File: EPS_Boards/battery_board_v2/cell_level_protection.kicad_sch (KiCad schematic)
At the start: 32 parts, among them J8 Shunt Resistor, Q10 CSD16401Q5, Q3 CSD16401Q5, Q4 CSD16401Q5, Q5 CSD16401Q5, Q6 CSD16401Q5, Q7 CSD16401Q5, Q8 CSD16401Q5, Q9 CSD16401Q5, U10 BQ297xx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

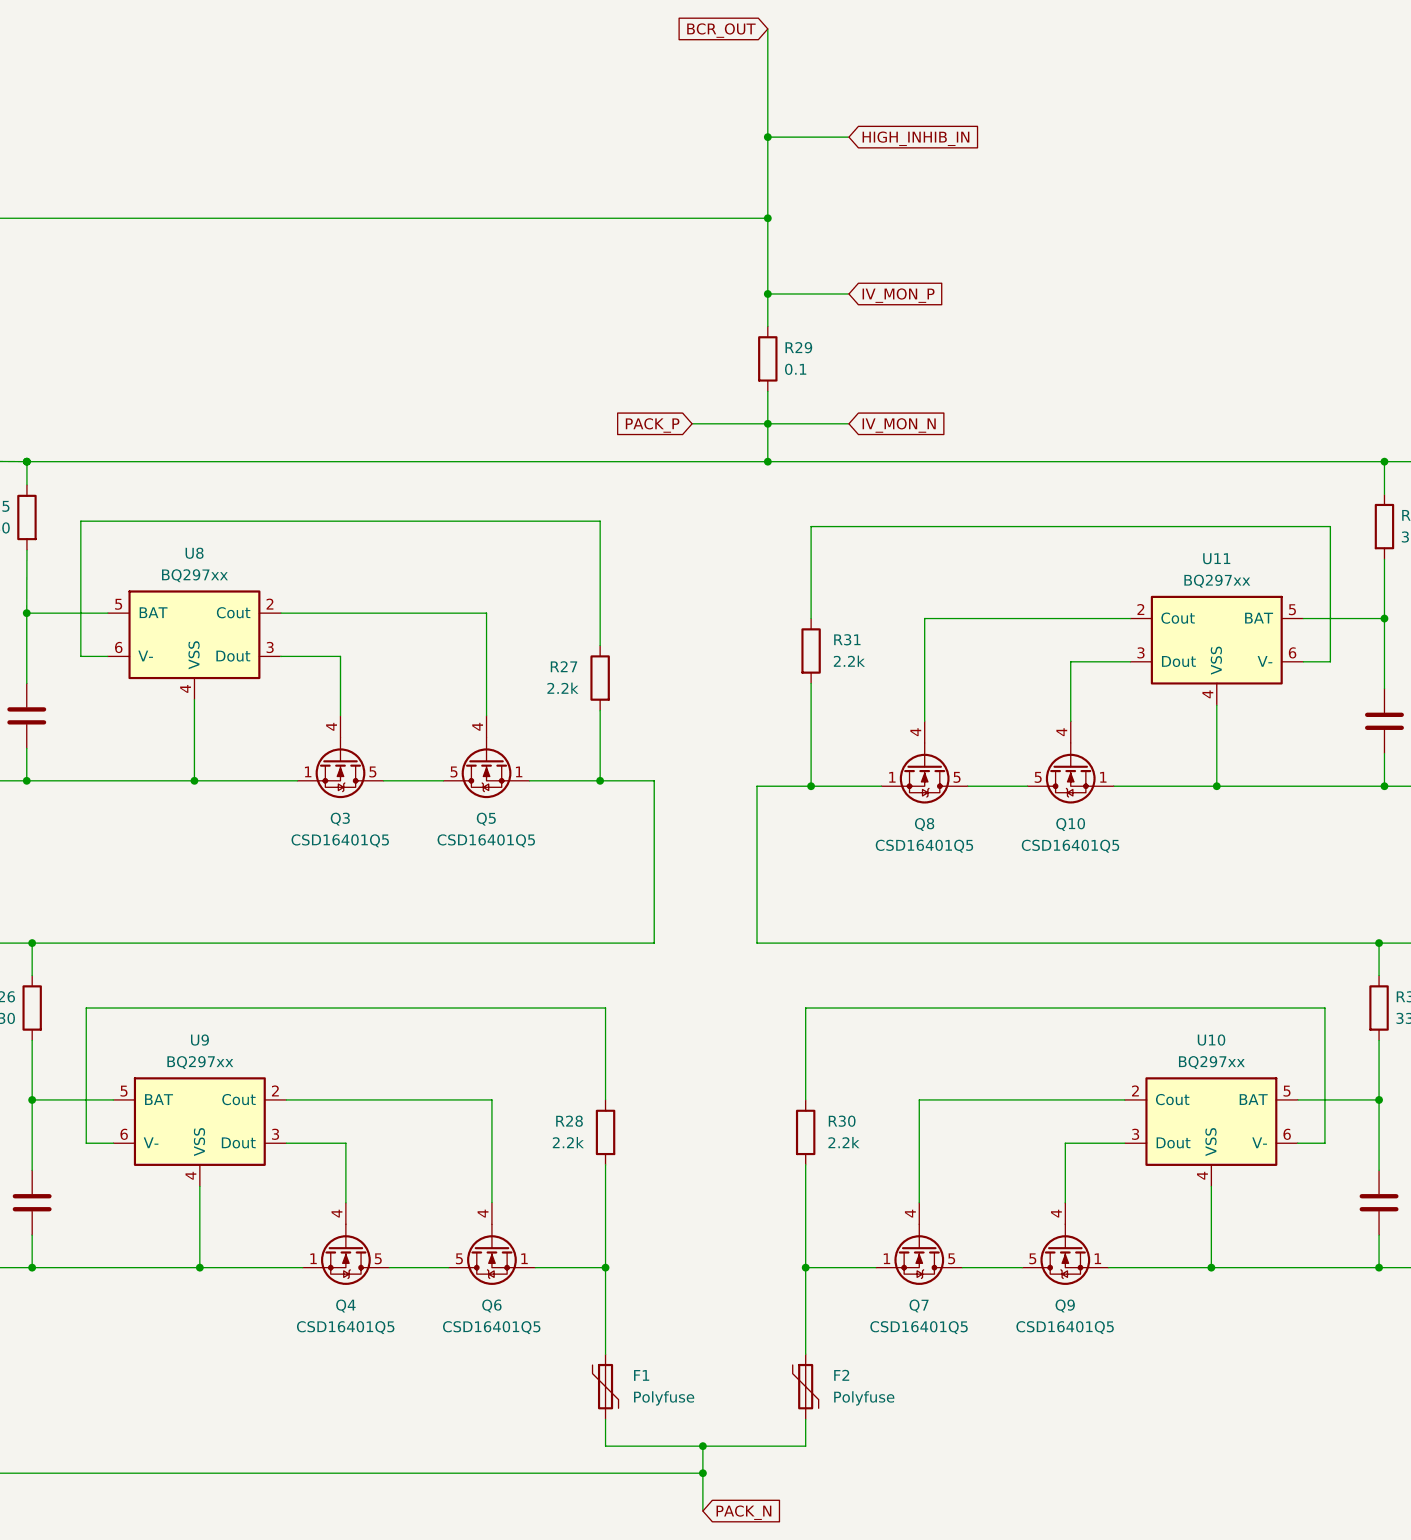
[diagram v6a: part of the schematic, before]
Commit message: eps: battery board: updated board layout
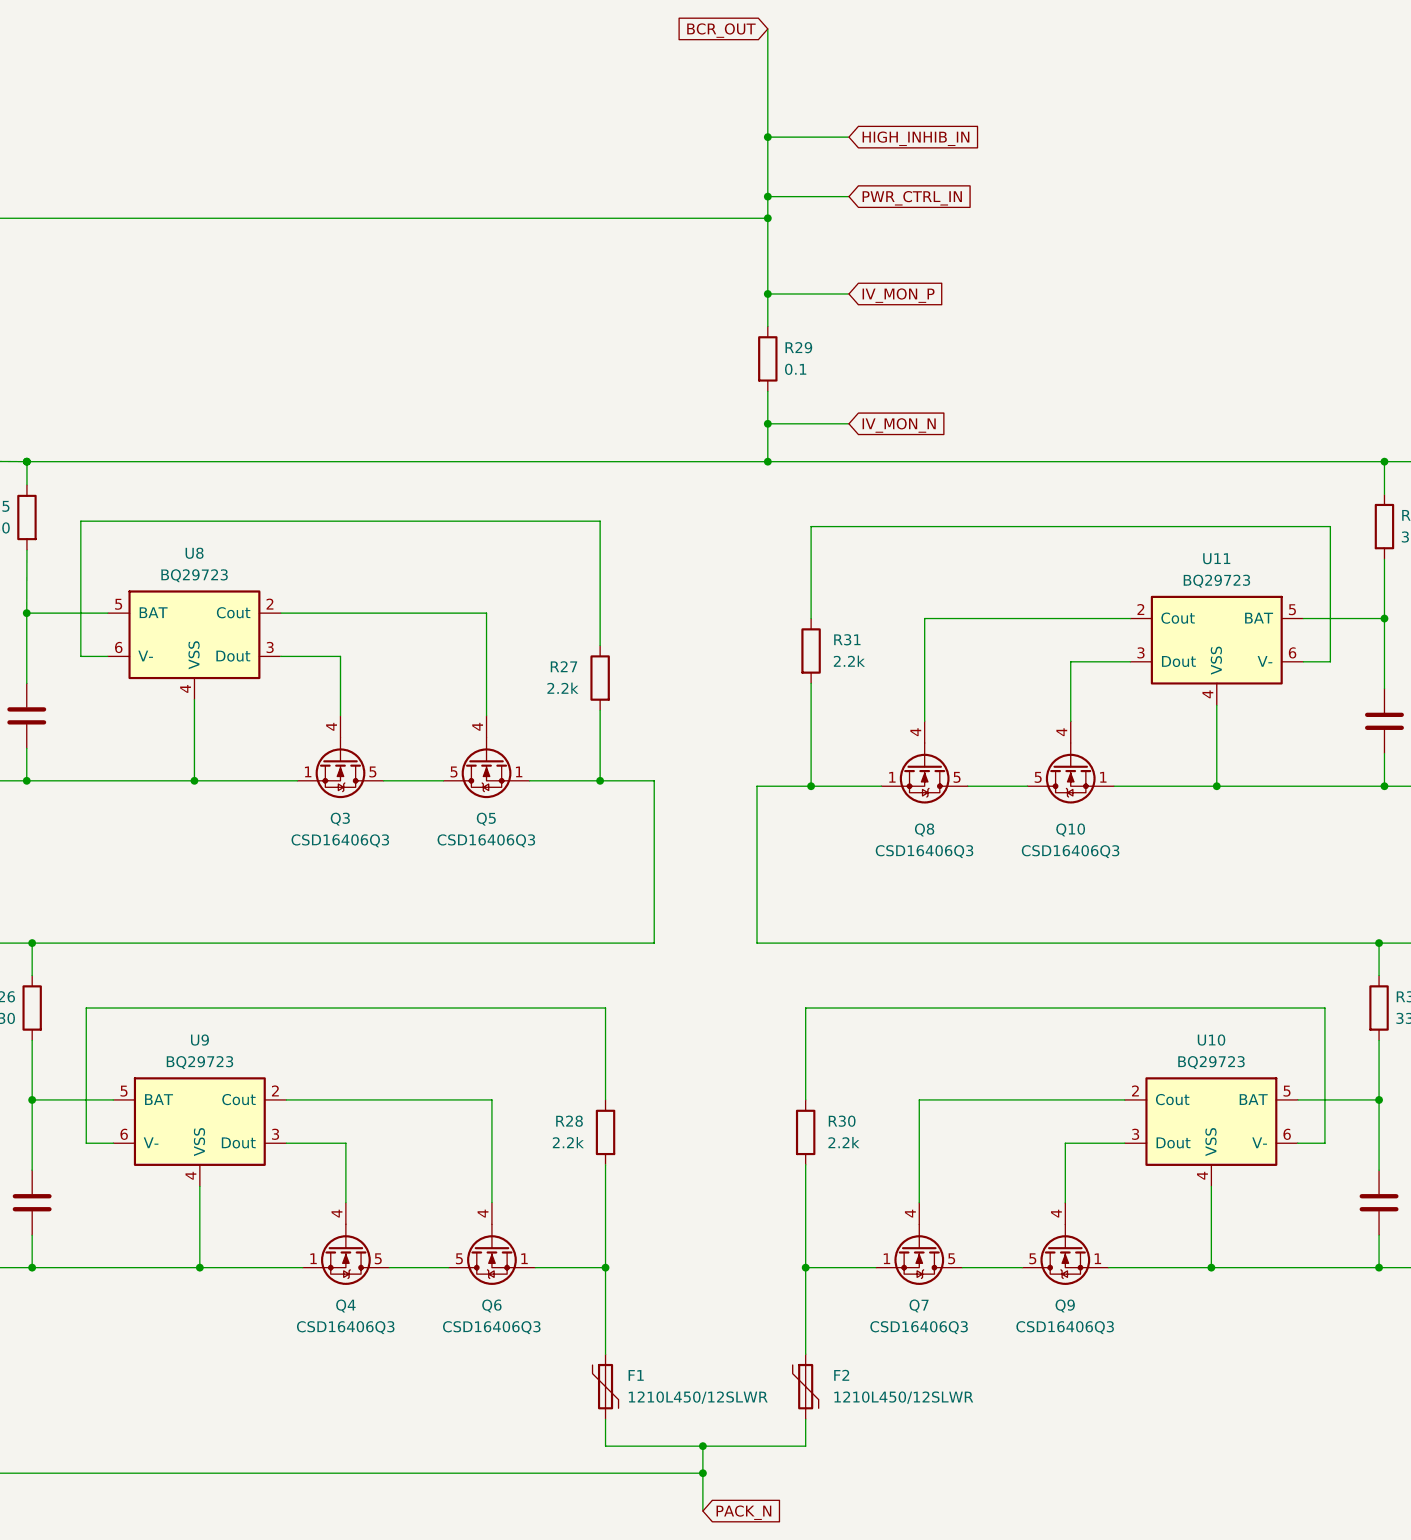
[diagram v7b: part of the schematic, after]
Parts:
- F1, F2: value Polyfuse -> 1210L450/12SLWR
- Q10, Q3, Q4, Q5, Q6, Q7, Q8, Q9: value CSD16401Q5 -> CSD16406Q3
- U10, U11, U8, U9: value BQ297xx -> BQ29723
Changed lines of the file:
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@@
   (junction (at 140.97 181.61) (diameter 0) (color 0 0 0 0)
   )
+  (junction (at 227.33 75.565) (diameter 0) (color 0 0 0 0)
+  )
   (junction (at 299.085 201.295) (diameter 0) (color 0 0 0 0)
   )
@@
     (stroke (width 0) (type default) (color 0 0 0 0))
   )
-  (wire (pts (xy 227.33 68.58) (xy 227.33 78.105))
+  (wire (pts (xy 227.33 68.58) (xy 227.33 75.565))
     (stroke (width 0) (type default) (color 0 0 0 0))
   )
@@
     (stroke (width 0) (type default) (color 0 0 0 0))
   )
+  (wire (pts (xy 227.33 75.565) (xy 236.855 75.565))
+    (stroke (width 0) (type default) (color 0 0 0 0))
+  )
   (wire (pts (xy 232.41 144.78) (xy 240.665 144.78))
     (stroke (width 0) (type default) (color 0 0 0 0))
@@
     (stroke (width 0) (type default) (color 0 0 0 0))
   )
+  (wire (pts (xy 227.33 75.565) (xy 227.33 78.105))
+    (stroke (width 0) (type default) (color 0 0 0 0))
+  )
   (wire (pts (xy 269.875 125.095) (xy 245.745 125.095))
     (stroke (width 0) (type default) (color 0 0 0 0))
@@
   )
   (wire (pts (xy 208.28 181.61) (xy 208.28 170.815))
-    (stroke (width 0) (type default) (color 0 0 0 0))
-  )
-  (wire (pts (xy 218.44 102.235) (xy 227.33 102.235))
     (stroke (width 0) (type default) (color 0 0 0 0))
   )
@@
     )
   )
-  (global_label "PACK_P" (shape input) (at 218.44 102.235 180) (fields_autoplaced)
-    (effects (font (size 1.27 1.27)) (justify right))
-    (property "Intersheet References" "${INTERSHEET_REFS}" (id 0) (at 208.8907 102.3144 0)
-      (effects (font (size 1.27 1.27)) (justify right) hide)
+  (global_label "PWR_CTRL_IN" (shape input) (at 236.855 75.565 0) (fields_autoplaced)
+    (effects (font (size 1.27 1.27)) (justify left))
+    (property "Intersheet References" "${INTERSHEET_REFS}" (id 0) (at 251.5768 75.4856 0)
+      (effects (font (size 1.27 1.27)) (justify left) hide)
     )
   )
@@
   (symbol (lib_id "Transistor_FET:CSD16401Q5") (at 245.745 142.24 270) (unit 1)
     (in_bom yes) (on_board yes) (fields_autoplaced)
-    (property "Reference" "Q8" (id 0) (at 245.745 149.225 90))
-    (property "Value" "CSD16401Q5" (id 1) (at 245.745 151.765 90))
+    (property "Reference" "Q8" (id 0) (at 245.745 149.86 90))
+    (property "Value" "CSD16406Q3" (id 1) (at 245.745 152.4 90))
     (property "Footprint" "Package_TO_SOT_SMD:TDSON-8-1" (id 2) (at 243.84 147.32 0)
       (effects (font (size 1.27 1.27) italic) (justify left) hide)
@@
     (in_bom yes) (on_board yes)
     (property "Reference" "U8" (id 0) (at 160.02 117.475 0))
-    (property "Value" "BQ297xx" (id 1) (at 160.02 120.015 0))
+    (property "Value" "BQ29723" (id 1) (at 160.02 120.015 0))
     (property "Footprint" "Package_SON:WSON-6_1.5x1.5mm_P0.5mm" (id 2) (at 160.02 118.11 0)
       (effects (font (size 1.27 1.27)) hide)
@@
     (in_bom yes) (on_board yes) (fields_autoplaced)
     (property "Reference" "Q5" (id 0) (at 194.31 148.59 90))
-    (property "Value" "CSD16401Q5" (id 1) (at 194.31 151.13 90))
+    (property "Value" "CSD16406Q3" (id 1) (at 194.31 151.13 90))
     (property "Footprint" "Package_TO_SOT_SMD:TDSON-8-1" (id 2) (at 196.215 146.685 0)
       (effects (font (size 1.27 1.27) italic) (justify left) hide)
@@
     (in_bom yes) (on_board yes) (fields_autoplaced)
     (property "Reference" "Q9" (id 0) (at 262.255 205.74 90))
-    (property "Value" "CSD16401Q5" (id 1) (at 262.255 208.28 90))
+    (property "Value" "CSD16406Q3" (id 1) (at 262.255 208.28 90))
     (property "Footprint" "Package_TO_SOT_SMD:TDSON-8-1" (id 2) (at 264.16 203.835 0)
       (effects (font (size 1.27 1.27) italic) (justify left) hide)
@@
     (in_bom yes) (on_board yes)
     (property "Reference" "U10" (id 0) (at 279.4 174.625 0))
-    (property "Value" "BQ297xx" (id 1) (at 279.4 177.165 0))
+    (property "Value" "BQ29723" (id 1) (at 279.4 177.165 0))
     (property "Footprint" "Package_SON:WSON-6_1.5x1.5mm_P0.5mm" (id 2) (at 279.4 175.26 0)
       (effects (font (size 1.27 1.27)) hide)
@@
     (in_bom yes) (on_board yes) (fields_autoplaced)
     (property "Reference" "Q7" (id 0) (at 245.11 205.74 90))
-    (property "Value" "CSD16401Q5" (id 1) (at 245.11 208.28 90))
+    (property "Value" "CSD16406Q3" (id 1) (at 245.11 208.28 90))
     (property "Footprint" "Package_TO_SOT_SMD:TDSON-8-1" (id 2) (at 243.205 203.835 0)
       (effects (font (size 1.27 1.27) italic) (justify left) hide)
@@
     (in_bom yes) (on_board yes) (fields_autoplaced)
     (property "Reference" "Q4" (id 0) (at 177.8 205.74 90))
-    (property "Value" "CSD16401Q5" (id 1) (at 177.8 208.28 90))
+    (property "Value" "CSD16406Q3" (id 1) (at 177.8 208.28 90))
     (property "Footprint" "Package_TO_SOT_SMD:TDSON-8-1" (id 2) (at 175.895 203.835 0)
       (effects (font (size 1.27 1.27) italic) (justify left) hide)
@@
     (in_bom yes) (on_board yes) (fields_autoplaced)
     (property "Reference" "Q3" (id 0) (at 177.165 148.59 90))
-    (property "Value" "CSD16401Q5" (id 1) (at 177.165 151.13 90))
+    (property "Value" "CSD16406Q3" (id 1) (at 177.165 151.13 90))
     (property "Footprint" "Package_TO_SOT_SMD:TDSON-8-1" (id 2) (at 175.26 146.685 0)
       (effects (font (size 1.27 1.27) italic) (justify left) hide)
@@
     (in_bom yes) (on_board yes)
     (property "Reference" "U9" (id 0) (at 160.655 174.625 0))
-    (property "Value" "BQ297xx" (id 1) (at 160.655 177.165 0))
+    (property "Value" "BQ29723" (id 1) (at 160.655 177.165 0))
     (property "Footprint" "Package_SON:WSON-6_1.5x1.5mm_P0.5mm" (id 2) (at 160.655 175.26 0)
       (effects (font (size 1.27 1.27)) hide)
@@
     (in_bom yes) (on_board yes)
     (property "Reference" "U11" (id 0) (at 280.035 118.11 0))
-    (property "Value" "BQ297xx" (id 1) (at 280.035 120.65 0))
+    (property "Value" "BQ29723" (id 1) (at 280.035 120.65 0))
     (property "Footprint" "Package_SON:WSON-6_1.5x1.5mm_P0.5mm" (id 2) (at 280.035 118.745 0)
       (effects (font (size 1.27 1.27)) hide)
@@
       (effects (font (size 1.27 1.27)) (justify left))
     )
-    (property "Value" "Polyfuse" (id 1) (at 234.95 216.5349 0)
+    (property "Value" "1210L450/12SLWR" (id 1) (at 234.95 216.5349 0)
       (effects (font (size 1.27 1.27)) (justify left))
     )
@@
     (in_bom yes) (on_board yes) (fields_autoplaced)
     (property "Reference" "Q6" (id 0) (at 194.945 205.74 90))
-    (property "Value" "CSD16401Q5" (id 1) (at 194.945 208.28 90))
+    (property "Value" "CSD16406Q3" (id 1) (at 194.945 208.28 90))
     (property "Footprint" "Package_TO_SOT_SMD:TDSON-8-1" (id 2) (at 196.85 203.835 0)
       (effects (font (size 1.27 1.27) italic) (justify left) hide)
@@
   (symbol (lib_id "Transistor_FET:CSD16401Q5") (at 262.89 142.24 90) (mirror x) (unit 1)
     (in_bom yes) (on_board yes) (fields_autoplaced)
-    (property "Reference" "Q10" (id 0) (at 262.89 149.225 90))
-    (property "Value" "CSD16401Q5" (id 1) (at 262.89 151.765 90))
+    (property "Reference" "Q10" (id 0) (at 262.89 149.86 90))
+    (property "Value" "CSD16406Q3" (id 1) (at 262.89 152.4 90))
     (property "Footprint" "Package_TO_SOT_SMD:TDSON-8-1" (id 2) (at 264.795 147.32 0)
       (effects (font (size 1.27 1.27) italic) (justify left) hide)
@@
   (symbol (lib_id "Device:Polyfuse") (at 208.28 215.265 0) (unit 1)
     (in_bom yes) (on_board yes) (fields_autoplaced)
-    (property "Reference" "F1" (id 0) (at 211.455 213.9949 0)
-      (effects (font (size 1.27 1.27)) (justify left))
-    )
-    (property "Value" "Polyfuse" (id 1) (at 211.455 216.5349 0)
-      (effects (font (size 1.27 1.27)) (justify left))
-    )
+    (property "Reference" "F1" (id 0) (at 210.82 213.9949 0)
+      (effects (font (size 1.27 1.27)) (justify left))
+    )
+    (property "Value" "1210L450/12SLWR" (id 1) (at 210.82 216.5349 0)
+      (effects (font (size 1.27 1.27)) (justify left))
+    )

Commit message: eps:battery:pcb layout
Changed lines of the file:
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@@
     (pin "2")
   )
-  (symbol (lib_id "Device:R") (at 299.72 114.3 0) (unit 1)
+  (symbol (lib_id "Device:R") (at 299.72 114.3 0) (mirror y) (unit 1)
     (in_bom yes) (on_board yes) (fields_autoplaced)
-    (property "Reference" "R33" (id 0) (at 301.625 113.0299 0)
-      (effects (font (size 1.27 1.27)) (justify left))
+    (property "Reference" "R33" (id 0) (at 302.26 113.0299 0)
+      (effects (font (size 1.27 1.27)) (justify right))
     )
-    (property "Value" "330" (id 1) (at 301.625 115.5699 0)
-      (effects (font (size 1.27 1.27)) (justify left))
+    (property "Value" "330" (id 1) (at 302.26 115.5699 0)
+      (effects (font (size 1.27 1.27)) (justify right))
     )
-    (property "Footprint" "Resistor_SMD:R_0402_1005Metric" (id 2) (at 297.942 114.3 90)
+    (property "Footprint" "Resistor_SMD:R_0402_1005Metric" (id 2) (at 301.498 114.3 90)
       (effects (font (size 1.27 1.27)) hide)
     )
